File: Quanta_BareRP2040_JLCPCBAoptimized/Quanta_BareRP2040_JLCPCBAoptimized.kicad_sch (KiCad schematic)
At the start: 253 parts, among them J1 USB_C_Receptacle_USB2.0, J10 Conn_01x05_Socket GPIOs, J2 Conn_01x02_Socket VBUS 5V, J3 Conn_01x02_Socket 3V3, J5 Conn_01x04_Socket SWD, J6 USB_A_Receptacle_UBS2.0, J7 USB_C_Receptacle_USB2.0, J8 Conn_01x04_Socket I2C display, J9 USB_C_Receptacle_USB2.0, SW1 SW_Push, SW10 SW_Push, SW11 SW_Push, SW12 SW_Push, SW13 SW_Push, SW14 SW_Push, SW15 SW_Push, SW16 SW_Push, SW17 SW_Push, SW18 SW_Push, SW19 SW_Push, SW2 SW_Push, SW20 SW_Push, SW21 SW_Push, SW22 SW_Push, SW23 SW_Push, SW24 SW_Push, SW25 SW_Push, SW26 SW_Push, SW27 SW_Push, SW28 SW_Push, SW29 SW_Push, SW3 SW_Push, SW30 SW_Push, SW31 SW_Push, SW32 SW_Push, SW33 SW_Push, SW34 SW_Push, SW35 SW_Push, SW36 SW_Push, SW37 SW_Push, SW38 SW_Push, SW39 SW_Push, SW4 SW_Push, SW40 SW_Push, SW41 SW_Push, SW42 SW_Push, SW43 SW_Push, SW44 SW_Push, SW45 SW_Push, SW46 SW_Push, SW47 SW_Push, SW48 SW_Push, SW49 SW_Push, SW5 SW_Push, SW50 SW_Push, SW51 SW_Push, SW52 SW_Push, SW53 SW_Push, SW54 SW_Push, SW55 SW_Push, SW56 SW_Push, SW57 SW_Push, SW58 SW_Push, SW59 SW_Push, SW6 SW_Push, SW60 SW_Push, SW61 SW_Push, SW62 SW_Push, SW63 SW_Push, SW64 SW_Push, SW65 SW_Push, SW66 SW_Push, SW67 SW_Push, SW68 SW_Push, SW69 SW_Push, SW7 SW_Push, SW70 SW_Push, SW71 SW_Push, SW72 SW_Push, SW73 SW_Push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

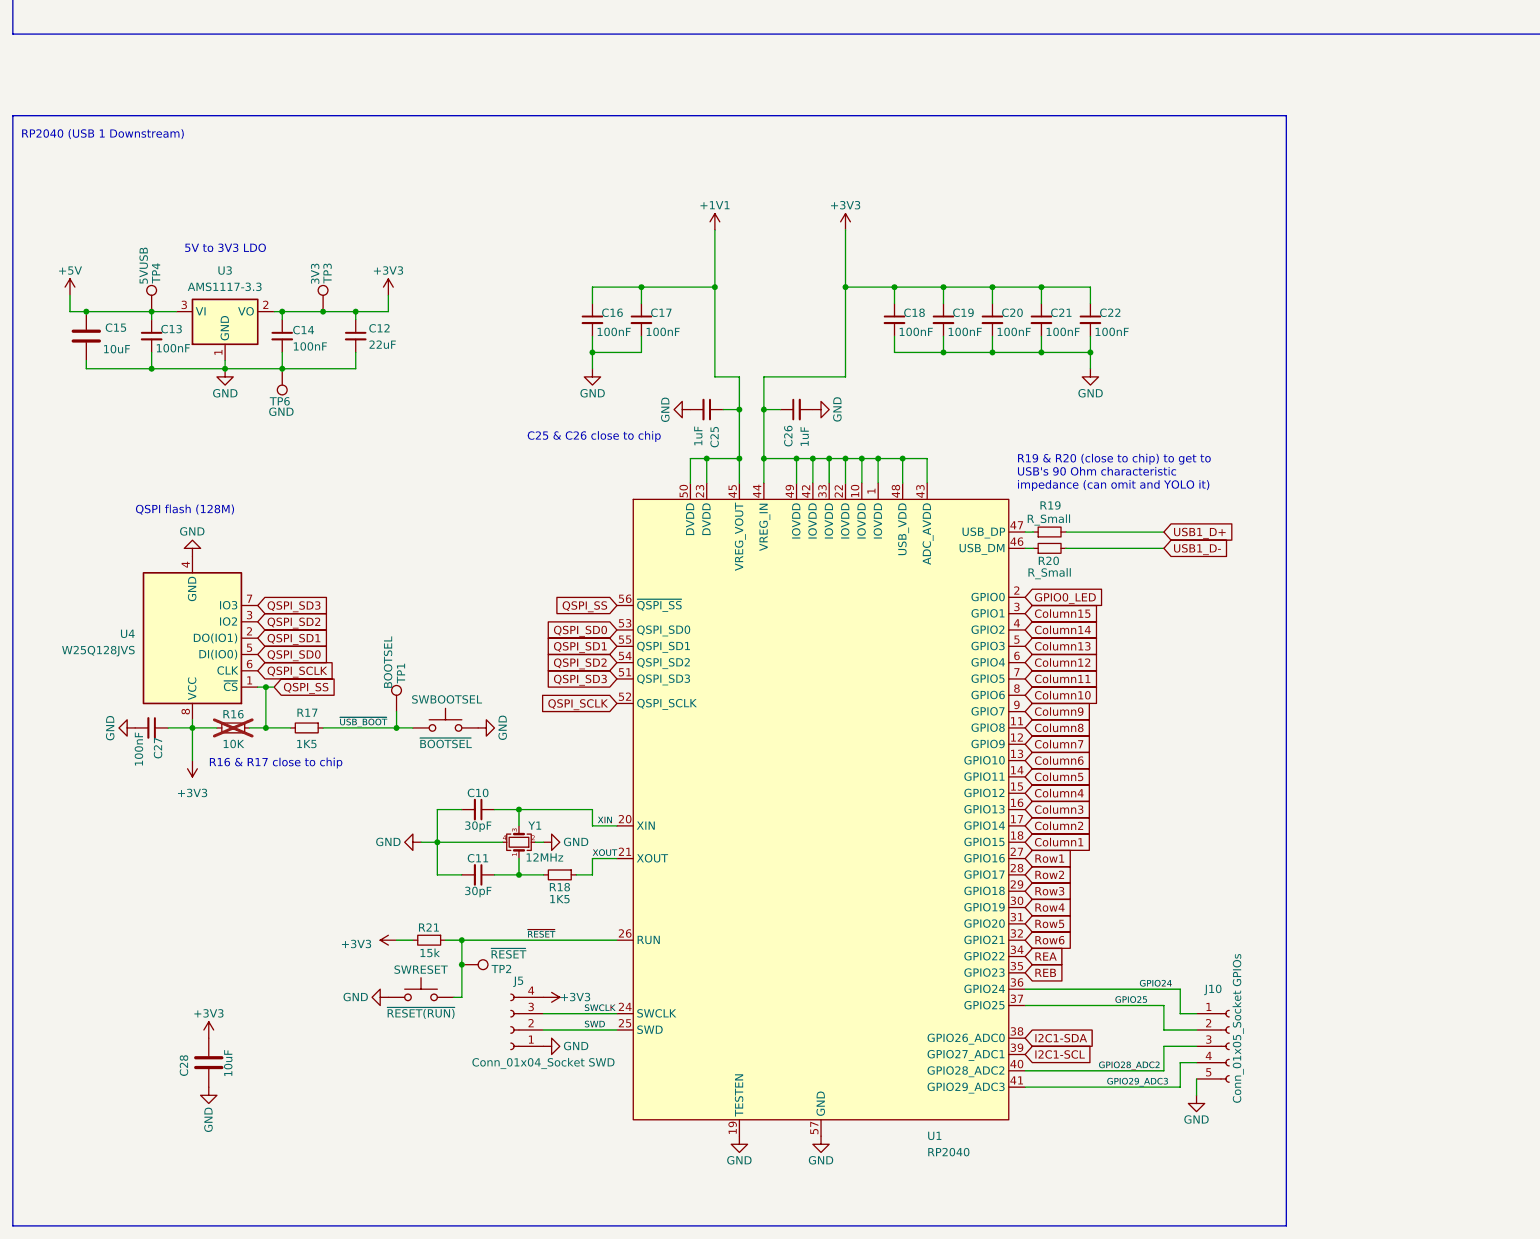
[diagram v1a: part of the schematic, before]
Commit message: update net label
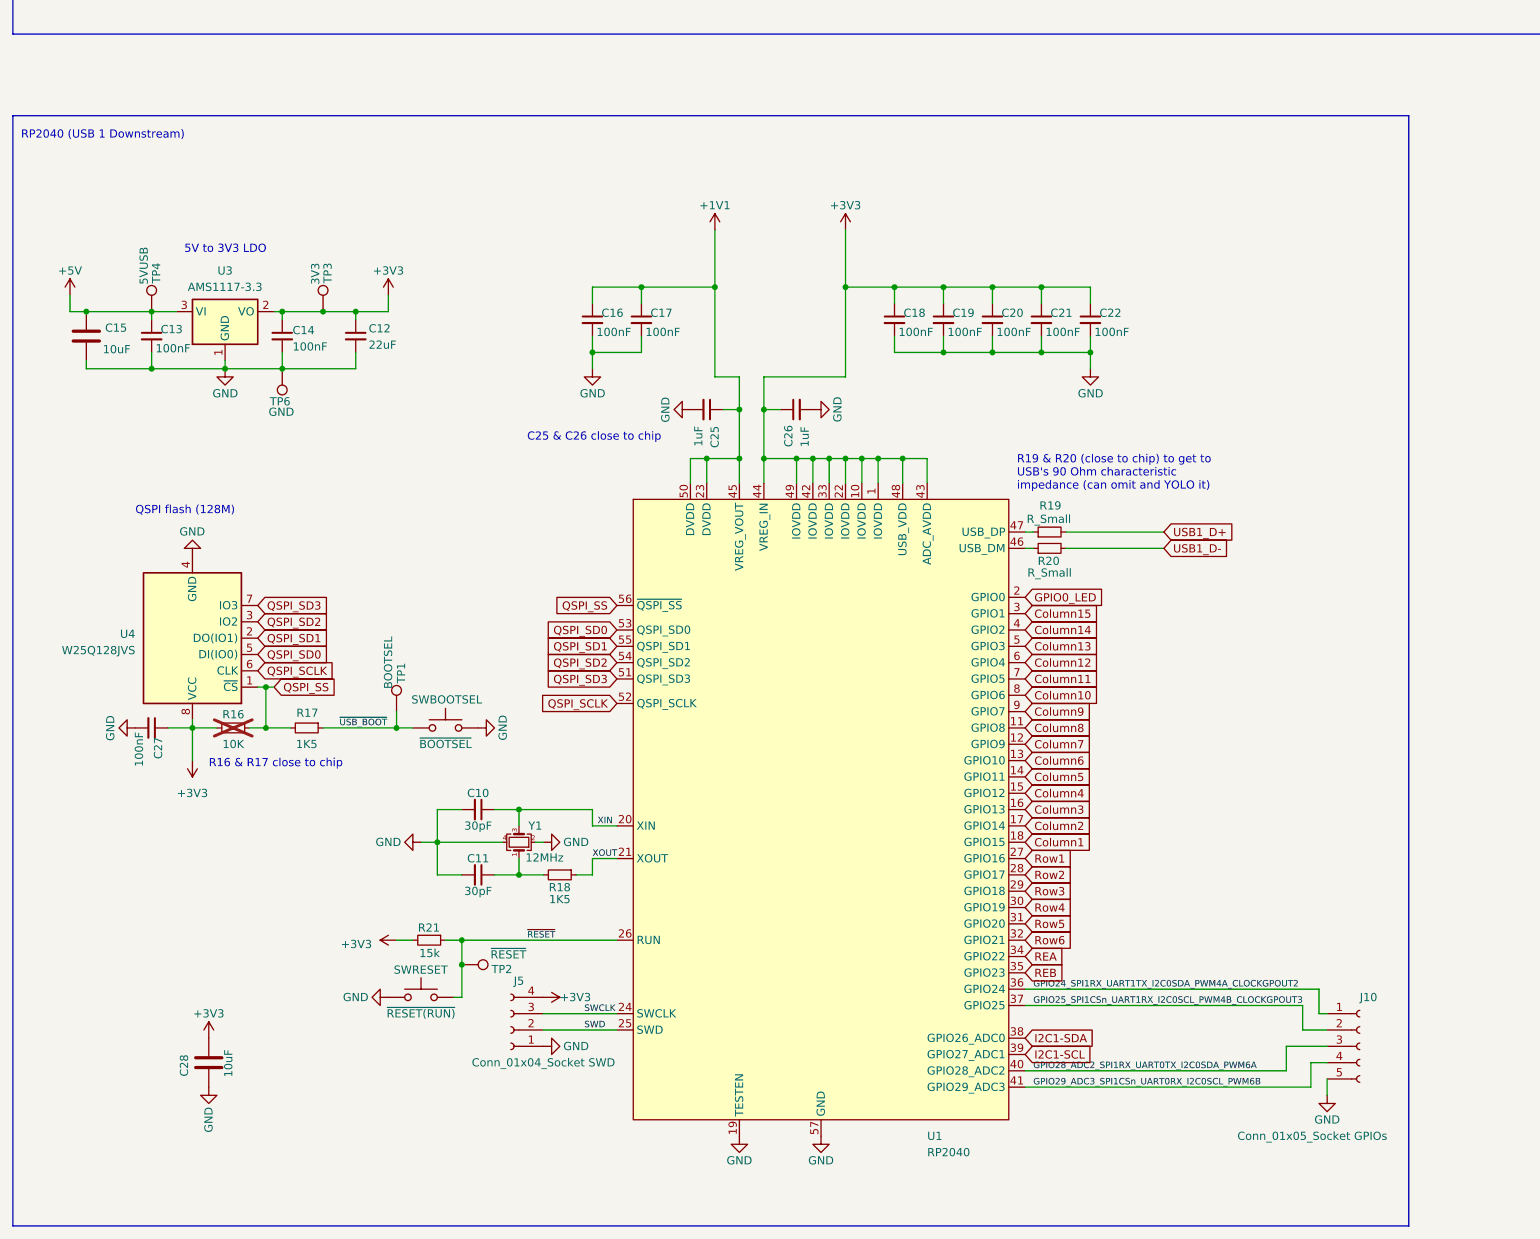
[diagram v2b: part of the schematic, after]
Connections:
- net GPIO24 renamed GPIO24_SPI1RX_UART1TX_I2C0SDA_PWM4A_CLOCKGPOUT2
- net GPIO25 renamed GPIO25_SPI1CSn_UART1RX_I2C0SCL_PWM4B_CLOCKGPOUT3
- net GPIO28_ADC2 renamed GPIO28_ADC2_SPI1RX_UART0TX_I2C0SDA_PWM6A
- net GPIO29_ADC3 renamed GPIO29_ADC3_SPI1CSn_UART0RX_I2C0SCL_PWM6B
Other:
- moved on the sheet: J10
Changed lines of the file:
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@@
     (stroke (width 0) (type default))
   )
-  (wire (pts (xy 209.55 354.33) (xy 212.09 354.33))
+  (wire (pts (xy 231.14 354.33) (xy 232.41 354.33))
     (stroke (width 0) (type default))
   )
@@
     (stroke (width 0) (type default))
   )
-  (wire (pts (xy 212.09 361.95) (xy 209.55 361.95))
+  (wire (pts (xy 232.41 361.95) (xy 229.87 361.95))
     (stroke (width 0) (type default))
   )
@@
     (stroke (width 0) (type default))
   )
-  (wire (pts (xy 212.09 356.87) (xy 207.01 356.87))
+  (wire (pts (xy 232.41 356.87) (xy 228.6 356.87))
     (stroke (width 0) (type default))
   )
@@
     (stroke (width 0) (type default))
   )
-  (wire (pts (xy 209.55 354.33) (xy 209.55 350.52))
+  (wire (pts (xy 231.14 354.33) (xy 231.14 350.52))
     (stroke (width 0) (type default))
   )
@@
     (stroke (width 0) (type default))
   )
-  (wire (pts (xy 185.42 353.06) (xy 207.01 353.06))
+  (wire (pts (xy 185.42 353.06) (xy 228.6 353.06))
     (stroke (width 0) (type default))
   )
@@
     (stroke (width 0) (type default))
   )
+  (wire (pts (xy 185.42 365.76) (xy 229.87 365.76))
+    (stroke (width 0) (type default))
+  )
   (wire (pts (xy 524.51 52.07) (xy 527.05 52.07))
     (stroke (width 0) (type default))
@@
     (stroke (width 0) (type default))
   )
-  (wire (pts (xy 185.42 350.52) (xy 209.55 350.52))
-    (stroke (width 0) (type default))
-  )
   (wire (pts (xy 506.73 260.35) (xy 509.27 260.35))
     (stroke (width 0) (type default))
@@
     (stroke (width 0) (type default))
   )
-  (wire (pts (xy 212.09 367.03) (xy 212.09 364.49))
-    (stroke (width 0) (type default))
-  )
   (wire (pts (xy 519.43 54.61) (xy 518.16 54.61))
     (stroke (width 0) (type default))
@@
     (stroke (width 0) (type default))
   )
-  (wire (pts (xy 185.42 365.76) (xy 209.55 365.76))
-    (stroke (width 0) (type default))
-  )
   (wire (pts (xy 180.34 241.3) (xy 172.72 241.3))
     (stroke (width 0) (type default))
@@
     (stroke (width 0) (type default))
   )
+  (wire (pts (xy 185.42 363.22) (xy 226.06 363.22))
+    (stroke (width 0) (type default))
+  )
   (wire (pts (xy 187.96 241.3) (xy 187.96 243.84))
     (stroke (width 0) (type default))
@@
     (stroke (width 0) (type default))
   )
-  (wire (pts (xy 207.01 356.87) (xy 207.01 353.06))
+  (wire (pts (xy 228.6 356.87) (xy 228.6 353.06))
     (stroke (width 0) (type default))
   )
@@
     (stroke (width 0) (type default))
   )
-  (wire (pts (xy 185.42 363.22) (xy 207.01 363.22))
-    (stroke (width 0) (type default))
-  )
   (wire (pts (xy 118.11 251.46) (xy 118.11 248.92))
     (stroke (width 0) (type default))
@@
     (stroke (width 0) (type default))
   )
+  (wire (pts (xy 185.42 350.52) (xy 231.14 350.52))
+    (stroke (width 0) (type default))
+  )
   (wire (pts (xy 115.57 40.64) (xy 132.08 40.64))
     (stroke (width 0) (type default))
@@
     (stroke (width 0) (type default))
   )
+  (wire (pts (xy 232.41 364.49) (xy 232.41 367.03))
+    (stroke (width 0) (type default))
+  )
   (wire (pts (xy 82.55 40.64) (xy 99.06 40.64))
     (stroke (width 0) (type default))
@@
     (stroke (width 0) (type default))
   )
-  (wire (pts (xy 207.01 359.41) (xy 207.01 363.22))
+  (wire (pts (xy 226.06 359.41) (xy 226.06 363.22))
     (stroke (width 0) (type default))
   )
@@
     (stroke (width 0) (type default))
   )
-  (wire (pts (xy 209.55 361.95) (xy 209.55 365.76))
+  (wire (pts (xy 229.87 361.95) (xy 229.87 365.76))
     (stroke (width 0) (type default))
   )
@@
     (stroke (width 0) (type default))
   )
-  (wire (pts (xy 212.09 359.41) (xy 207.01 359.41))
+  (wire (pts (xy 232.41 359.41) (xy 226.06 359.41))
     (stroke (width 0) (type default))
   )
@@
     (fill (type none))
   )
-  (rectangle (start 27.94 214.63) (end 226.06 387.35)
+  (rectangle (start 27.94 214.63) (end 245.11 387.35)
     (stroke (width 0) (type default))
     (fill (type none))
@@
     (effects (font (size 1 1)) (justify left bottom))
   )
-  (label "GPIO28_ADC2" (at 196.85 363.22 0) (fields_autoplaced)
+  (label "GPIO28_ADC2_SPI1RX_UART0TX_I2C0SDA_PWM6A" (at 186.69 363.22 0) (fields_autoplaced)
     (effects (font (size 1 1)) (justify left bottom))
   )
-  (label "GPIO29_ADC3" (at 198.12 365.76 0) (fields_autoplaced)
+  (label "GPIO29_ADC3_SPI1CSn_UART0RX_I2C0SCL_PWM6B" (at 186.69 365.76 0) (fields_autoplaced)
     (effects (font (size 1 1)) (justify left bottom))
   )
@@
     (effects (font (size 1.27 1.27)) (justify left bottom))
   )
-  (label "GPIO24" (at 203.2 350.52 0) (fields_autoplaced)
+  (label "GPIO24_SPI1RX_UART1TX_I2C0SDA_PWM4A_CLOCKGPOUT2" (at 186.69 350.52 0) (fields_autoplaced)
     (effects (font (size 1 1)) (justify left bottom))
   )
@@
     (effects (font (size 1.27 1.27)) (justify left bottom))
   )
-  (label "GPIO25" (at 199.39 353.06 0) (fields_autoplaced)
+  (label "GPIO25_SPI1CSn_UART1RX_I2C0SCL_PWM4B_CLOCKGPOUT3" (at 186.69 353.06 0) (fields_autoplaced)
     (effects (font (size 1 1)) (justify left bottom))
   )
@@
     )
   )
-  (symbol (lib_id "Connector:Conn_01x05_Socket") (at 217.17 359.41 0) (unit 1)
+  (symbol (lib_id "Connector:Conn_01x05_Socket") (at 237.49 359.41 0) (unit 1)
     (in_bom yes) (on_board yes) (dnp no)
-    (property "Reference" "J10" (at 213.36 350.52 0)
+    (property "Reference" "J10" (at 237.49 351.79 0)
       (effects (font (size 1.27 1.27)) (justify left))
     )
-    (property "Value" "Conn_01x05_Socket GPIOs" (at 218.44 368.3 90)
+    (property "Value" "Conn_01x05_Socket GPIOs" (at 218.44 373.38 0)
       (effects (font (size 1.27 1.27)) (justify left))
     )
-    (property "Footprint" "Connector_PinHeader_2.54mm:PinHeader_1x05_P2.54mm_Vertical" (at 217.17 359.41 0)
+    (property "Footprint" "Connector_PinHeader_2.54mm:PinHeader_1x05_P2.54mm_Vertical" (at 237.49 359.41 0)
       (effects (font (size 1.27 1.27)) hide)
     )
-    (property "Datasheet" "~" (at 217.17 359.41 0)
+    (property "Datasheet" "~" (at 237.49 359.41 0)
       (effects (font (size 1.27 1.27)) hide)
     )
@@
     )
   )
-  (symbol (lib_id "power:GND") (at 212.09 367.03 0) (unit 1)
+  (symbol (lib_id "power:GND") (at 232.41 367.03 0) (unit 1)
     (in_bom yes) (on_board yes) (dnp no)
-    (property "Reference" "#PWR031" (at 212.09 373.38 0)
+    (property "Reference" "#PWR031" (at 232.41 373.38 0)
       (effects (font (size 1.27 1.27)) hide)
     )
-    (property "Value" "GND" (at 212.09 370.84 0)
+    (property "Value" "GND" (at 232.41 370.84 0)
       (effects (font (size 1.27 1.27)))
     )
-    (property "Footprint" "" (at 212.09 367.03 0)
+    (property "Footprint" "" (at 232.41 367.03 0)
       (effects (font (size 1.27 1.27)) hide)
     )
-    (property "Datasheet" "" (at 212.09 367.03 0)
+    (property "Datasheet" "" (at 232.41 367.03 0)
       (effects (font (size 1.27 1.27)) hide)
     )
